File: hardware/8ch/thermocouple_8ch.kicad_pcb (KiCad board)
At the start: 4 copper layers, 250 x 140 mm, 208 parts, among them J1 24V_INPUT, J2 LCD_16x2_HEADER, J3 RELAY_COM_NO_NC, J4 RS485_A_B_GND_SHIELD, J5 AVR_ISP, J6 MCU_EXPANSION, K1 G5LE-1 DC24, Q1 2N7000, SW1 NEXT, SW2 UP, SW3 DOWN, SW4 SET, SW5 ACK, U1 ATmega32A-PU, U10 ISO7760FDWR, U11 ISO7761FDWR, U12 IA0505S, U13 LP2985-3.3, U14 LM5164DDAR, U15 ADM2587EBRWZ, U2 MAX31856MUD+, U3 MAX31856MUD+, U4 MAX31856MUD+, U5 MAX31856MUD+, U6 MAX31856MUD+, U7 MAX31856MUD+, U8 MAX31856MUD+, U9 MAX31856MUD+, Y1 8MHz 20pF

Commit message: Hierarchical schematic; U12 decoupling fixed; two blind gates fixed (I-062, I-045)
Schematic (I-062, decision 0019): an A3 root plus channel.kicad_sch (A4)
used by sheets TC1-TC8, derived by sch_layout/hier.py as the last step of
build.py. Only channel-internal nets were renamed (/TCn_X -> /TCn/X, 40
nets); JTC1-8 value -> K_TYPE (KiCad 10 keeps one value per symbol).
netlist_fingerprint.py --allow-renames proved all 645 pins on the same
nets; the baseline was regenerated from that netlist with the reason in it.
apply_rules.py patterns follow (without them: 499 isolation violations on a
test copy); board nets renamed in place by rename_board_nets.py.

Board (I-045): C45, U12's input cap, sat 55 mm away beside U10; C45/C46 now
sit under U12's pins, 18/10 mm -> 4.2 mm. Re-routed.

Gates that passed on the wrong input: close_gaps.py read a 2026-09-07 DRC
report (now runs its own with --refill-zones); check_mpn_consistency.py read
only the root after the split, 56 of 128 symbols (now follows every sheet
and runs inside validate.ps1, I-054 downgraded). populate_schematic.py
refuses the hierarchical root.

validate.ps1, KiCad 10.0.6: ERC 0/0, netlist IDENTICAL 201/162/645, MPN
128/128, DRC 0 errors / 0 warnings / 0 unconnected / 0 parity.
check_board.py all 6 ok. firmware/build.ps1: 3 suites pass.

Co-Authored-By: Claude Opus 5.5 <noreply@anthropic.com>
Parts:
- JTC1: value TC1_K_TYPE -> K_TYPE
- JTC2: value TC2_K_TYPE -> K_TYPE
- JTC3: value TC3_K_TYPE -> K_TYPE
- JTC4: value TC4_K_TYPE -> K_TYPE
- JTC5: value TC5_K_TYPE -> K_TYPE
- JTC6: value TC6_K_TYPE -> K_TYPE
- JTC7: value TC7_K_TYPE -> K_TYPE
- JTC8: value TC8_K_TYPE -> K_TYPE
- moved C45 58.8 mm to (153.2, 104.2), turned to 180 degrees
- moved C46 9.04 mm to (143.0, 104.2)
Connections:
- net /MISO_CH1 renamed /TC1/MISO_CH
- net /MISO_CH2 renamed /TC2/MISO_CH
- net /MISO_CH3 renamed /TC3/MISO_CH
- net /MISO_CH4 renamed /TC4/MISO_CH
- net /MISO_CH5 renamed /TC5/MISO_CH
- net /MISO_CH6 renamed /TC6/MISO_CH
- net /MISO_CH7 renamed /TC7/MISO_CH
- net /MISO_CH8 renamed /TC8/MISO_CH
- net /TC1_FILT_N renamed /TC1/FILT_N
- net /TC1_FILT_P renamed /TC1/FILT_P
- net /TC1_RAW_N renamed /TC1/RAW_N
- net /TC1_RAW_P renamed /TC1/RAW_P
- net /TC2_FILT_N renamed /TC2/FILT_N
- net /TC2_FILT_P renamed /TC2/FILT_P
- net /TC2_RAW_N renamed /TC2/RAW_N
- net /TC2_RAW_P renamed /TC2/RAW_P
- net /TC3_FILT_N renamed /TC3/FILT_N
- net /TC3_FILT_P renamed /TC3/FILT_P
- net /TC3_RAW_N renamed /TC3/RAW_N
- net /TC3_RAW_P renamed /TC3/RAW_P
- net /TC4_FILT_N renamed /TC4/FILT_N
- net /TC4_FILT_P renamed /TC4/FILT_P
- net /TC4_RAW_N renamed /TC4/RAW_N
- net /TC4_RAW_P renamed /TC4/RAW_P
- net /TC5_FILT_N renamed /TC5/FILT_N
- net /TC5_FILT_P renamed /TC5/FILT_P
- net /TC5_RAW_N renamed /TC5/RAW_N
- net /TC5_RAW_P renamed /TC5/RAW_P
- net /TC6_FILT_N renamed /TC6/FILT_N
- net /TC6_FILT_P renamed /TC6/FILT_P
- net /TC6_RAW_N renamed /TC6/RAW_N
- net /TC6_RAW_P renamed /TC6/RAW_P
- net /TC7_FILT_N renamed /TC7/FILT_N
- net /TC7_FILT_P renamed /TC7/FILT_P
- net /TC7_RAW_N renamed /TC7/RAW_N
- net /TC7_RAW_P renamed /TC7/RAW_P
- net /TC8_FILT_N renamed /TC8/FILT_N
- net /TC8_FILT_P renamed /TC8/FILT_P
- net /TC8_RAW_N renamed /TC8/RAW_N
- net /TC8_RAW_P renamed /TC8/RAW_P
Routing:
- net /CS7_SENS: track 77.8 -> 98.3 mm
- net /SPARE_PC4: track 63.0 -> 52.5 mm, vias 2 -> 0
- net /CS6_SENS: track 106.4 -> 116.1 mm
- net /CS8_SENS: track 70.6 -> 62.1 mm
- net /SPARE_PC5: track 53.3 -> 45.2 mm, vias 1 -> 0
- net /CS6_CTRL: track 87.5 -> 80.2 mm
- net /CS7_CTRL: track 67.2 -> 60.5 mm, vias 1 -> 0
- net /CS8_CTRL: track 64.9 -> 58.4 mm
- net /CS1_CTRL: track 32.9 -> 27.4 mm, vias 2 -> 1
- net /MISO_SENS: track 313.6 -> 308.5 mm, vias 9 -> 11
- net /GND_CTRL: track 81.8 -> 85.4 mm, vias 4 -> 5
- net /SCK_SENS: track 342.6 -> 346.0 mm, vias 11 -> 10
- net /MOSI_CTRL: track 58.8 -> 55.6 mm
- net /SCK_CTRL: track 66.5 -> 63.5 mm, vias 2 -> 1
- net /CS3_CTRL: track 36.5 -> 33.6 mm, vias 2 -> 0
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
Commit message: Close I-027 from the MAX31856 datasheet; silkscreen said REV A0 on REV A1
MAX31856 datasheet 19-7534 Rev 0 added (from LCSC C116632; analog.com resets
the workstation's connection). "T- is biased to approximately 0.735V by the
BIAS output" and the typical circuit is a floating thermocouple with BIAS on
T-, which every channel already has; BIAS floats between conversions and the
bank driver runs continuous mode. Ungrounded probes need no extra resistor.

The REV A1 board carried "THERMO-8CH REV A0" on its silkscreen: BOARD_REV was
never bumped. Now A1; place_labels() rewrites the revision line so
generate_board.py --silk-only carries a bump to a routed board.

validate.ps1: ERC 0/0, netlist IDENTICAL, MPN 128/128, DRC 0/0/0/0.

Co-Authored-By: Claude Opus 5.5 <noreply@anthropic.com>
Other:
- board text added: "THERMO-8CH REV A1 2026-09"
- board text removed: "THERMO-8CH REV A0 2026-09"
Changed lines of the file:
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@@
 		(tags "THT Terminal Block Phoenix MKDS-1,5-3 pitch 5mm size 15x9.8mm drill 1.3mm pad 2.6mm")
 		(property "Reference" "J3"
-			(at 5 -6.665 0)
+			(at 13.875 -0.305 0)
 			(layer "F.SilkS")
 			(effects
@@
 		)
 	)
-	(gr_text "THERMO-8CH  REV A0  2026-09"
+	(gr_text "THERMO-8CH  REV A1  2026-09"
 		(at 70 56.5 0)
 		(layer "F.SilkS")
@@
 	)
 	(gr_text "RUN-PERMIT\nDRY CONTACT"
-		(at 240.5 67.5 0)
+		(at 240.5 63.75 0)
 		(layer "F.SilkS")
 		(effects
@@
 	)
 	(gr_text "LOW-VOLTAGE\nLOAD ONLY"
-		(at 240.5 70.75 0)
+		(at 240.5 67 0)
 		(layer "F.SilkS")
 		(effects

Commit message: Schematic on six A4 sheets by function (0021); external panel fuse specified (0020)
The root's remaining blocks move to power, mcu, isolation and relay_rs485
sheets; the root becomes an A4 index beside the reused channel sheet.
56 sheet-internal nets gain the sheet path. apply_rules.py patterns and
board/units.bare() follow, and all 162 board nets keep their netclass.
Board nets renamed in place, copper unchanged. validate.ps1: ERC 0/0,
netlist IDENTICAL, MPN 128/128, DRC 0/0/0/0; check_board all ok; build.py
reproduces the six sheets.

I-028 (a): external 1 A time-delay DC fuse, >= 80 V DC, >= 10 kA, at the
battery end; inrush in CALCULATIONS.md 1.9. New low I-064 (board overlaps
its PCB-editor page frame, cosmetic).

Co-Authored-By: Claude Opus 5.5 <noreply@anthropic.com>
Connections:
- net /+24V_FUSED renamed /POWER/+24V_FUSED
- net /+24V_RAW renamed /POWER/+24V_RAW
- net /+5V_ISO renamed /ISOLATION/+5V_ISO
- net /+5V_RS485 renamed /RELAY_RS485/+5V_RS485
- net /AREF renamed /MCU/AREF
- net /BST_5V renamed /POWER/BST_5V
- net /BTN_ACK renamed /MCU/BTN_ACK
- net /BTN_DOWN renamed /MCU/BTN_DOWN
- net /BTN_NEXT renamed /MCU/BTN_NEXT
- net /BTN_SET renamed /MCU/BTN_SET
- net /BTN_UP renamed /MCU/BTN_UP
- net /CS1_SENS_RAW renamed /ISOLATION/CS1_SENS_RAW
- net /CS2_SENS_RAW renamed /ISOLATION/CS2_SENS_RAW
- net /CS3_SENS_RAW renamed /ISOLATION/CS3_SENS_RAW
- net /CS4_SENS_RAW renamed /ISOLATION/CS4_SENS_RAW
- net /CS5_SENS_RAW renamed /ISOLATION/CS5_SENS_RAW
- net /CS6_SENS_RAW renamed /ISOLATION/CS6_SENS_RAW
- net /CS7_SENS_RAW renamed /ISOLATION/CS7_SENS_RAW
- net /CS8_SENS_RAW renamed /ISOLATION/CS8_SENS_RAW
- net /FB_5V renamed /POWER/FB_5V
- net /GND_RS485 renamed /RELAY_RS485/GND_RS485
- net /LCD_D4 renamed /MCU/LCD_D4
- net /LCD_D5 renamed /MCU/LCD_D5
- net /LCD_D6 renamed /MCU/LCD_D6
- net /LCD_D7 renamed /MCU/LCD_D7
- net /LCD_E renamed /MCU/LCD_E
- net /LCD_LED_A renamed /MCU/LCD_LED_A
- net /LCD_RS renamed /MCU/LCD_RS
- net /LCD_VO renamed /MCU/LCD_VO
- net /MISO_SENS_RAW renamed /ISOLATION/MISO_SENS_RAW
- net /MOSI_SENS_RAW renamed /ISOLATION/MOSI_SENS_RAW
- net /RELAY_COM renamed /RELAY_RS485/RELAY_COM
- net /RELAY_GATE renamed /RELAY_RS485/RELAY_GATE
- net /RELAY_LED_A renamed /RELAY_RS485/RELAY_LED_A
- net /RELAY_LOW renamed /RELAY_RS485/RELAY_LOW
- net /RELAY_NC renamed /RELAY_RS485/RELAY_NC
- net /RELAY_NO renamed /RELAY_RS485/RELAY_NO
- net /RESET_N renamed /MCU/RESET_N
- net /RIPPLE_INJ renamed /POWER/RIPPLE_INJ
- net /RON_SET renamed /POWER/RON_SET
- net /RS485_A renamed /RELAY_RS485/RS485_A
- net /RS485_B renamed /RELAY_RS485/RS485_B
- net /RS485_BIAS_A renamed /RELAY_RS485/RS485_BIAS_A
- net /RS485_BIAS_B renamed /RELAY_RS485/RS485_BIAS_B
- net /RS485_RE_N renamed /RELAY_RS485/RS485_RE_N
- net /RS485_TERM_A renamed /RELAY_RS485/RS485_TERM_A
- net /SCK_SENS_RAW renamed /ISOLATION/SCK_SENS_RAW
- net /SPARE_PA2 renamed /MCU/SPARE_PA2
- net /SPARE_PA3 renamed /MCU/SPARE_PA3
- net /SPARE_PC3 renamed /MCU/SPARE_PC3
- net /SPARE_PC4 renamed /MCU/SPARE_PC4
- net /SPARE_PC5 renamed /MCU/SPARE_PC5
- net /SW_5V renamed /POWER/SW_5V
- net /VIN_UVLO renamed /POWER/VIN_UVLO
- net /XTAL1 renamed /MCU/XTAL1
- net /XTAL2 renamed /MCU/XTAL2

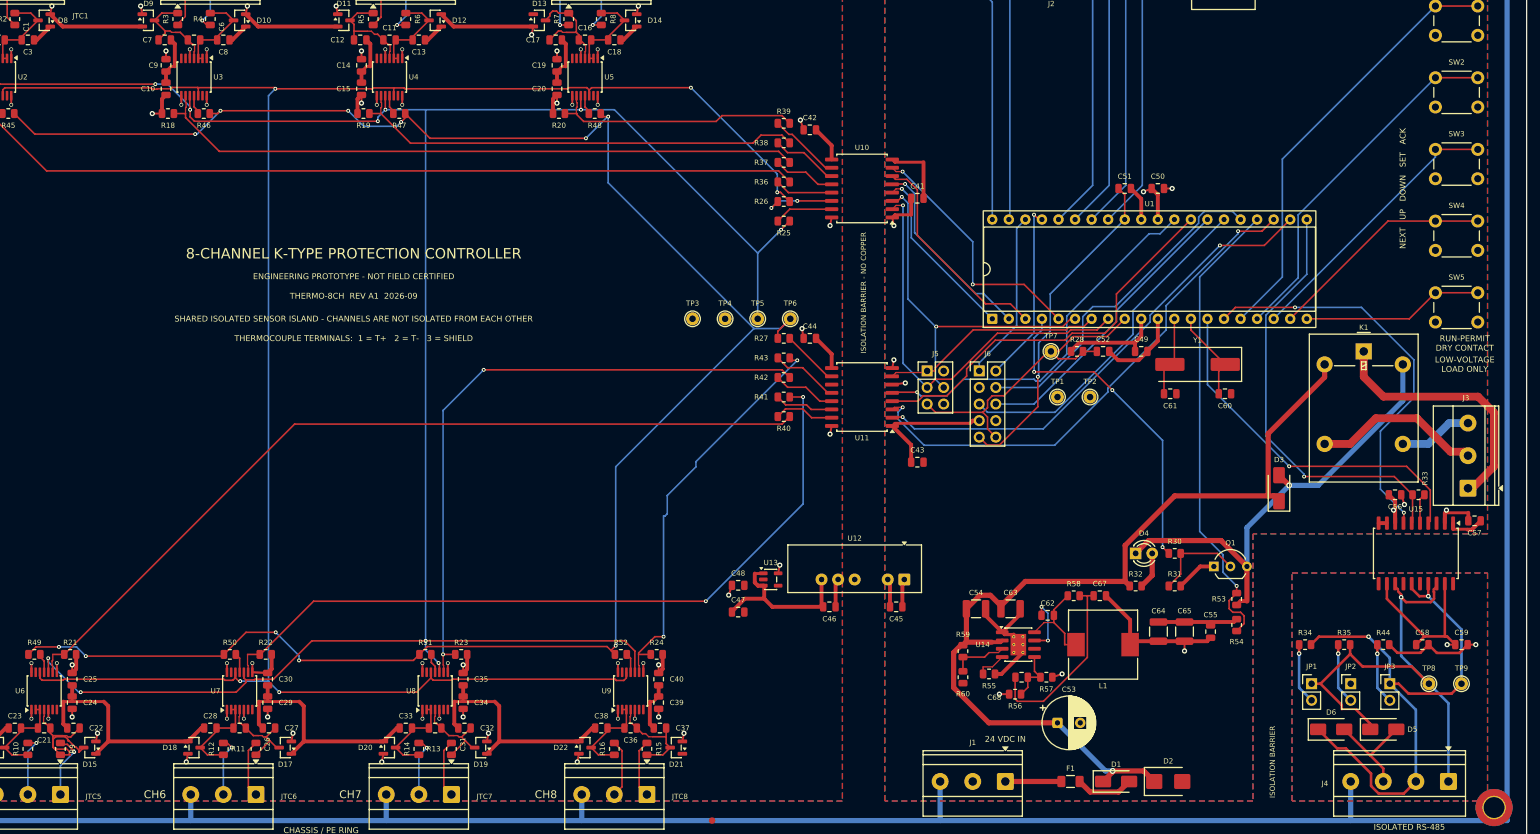
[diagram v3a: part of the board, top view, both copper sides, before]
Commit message: REV A2: pre-fabrication fixes I-065..I-069 (decision 0022)
- U10/U11 ISO7760DWR/ISO7761DWR (no F: open input -> HIGH) + R61 2k2 on
  U11 OUTF -> MISO_CTRL so in-circuit ISP works (I-065)
- Q1 BSS131 240 V SOT-23 replaces the 60 V 2N7000 (I-066)
- R53/R54 100k/22k: 0.28 mA into PC2's clamp at 58 V (I-067)
- F1 1812L075/60GR, 60 V 0.75 A 1812 (I-068)
- D2 drawn unidirectional, D3 = M7 SMA, U12 sourcing warning (I-069)
- netlist-baseline-reva2.json (202/163/647), BOARD_REV A2
- board regenerated and re-routed; one hand via for C41.1 (+5V_CTRL)
- run_all.ps1 no longer calls populate_schematic.py (hierarchical sheet)

validate.ps1 2026-09-28 01:07: ERC 0/0, netlist IDENTICAL, DRC 0/0/0/0;
check_board.py all 6 ok; firmware build + 3 suites pass.

Co-Authored-By: Claude Opus 5.5 <noreply@anthropic.com>
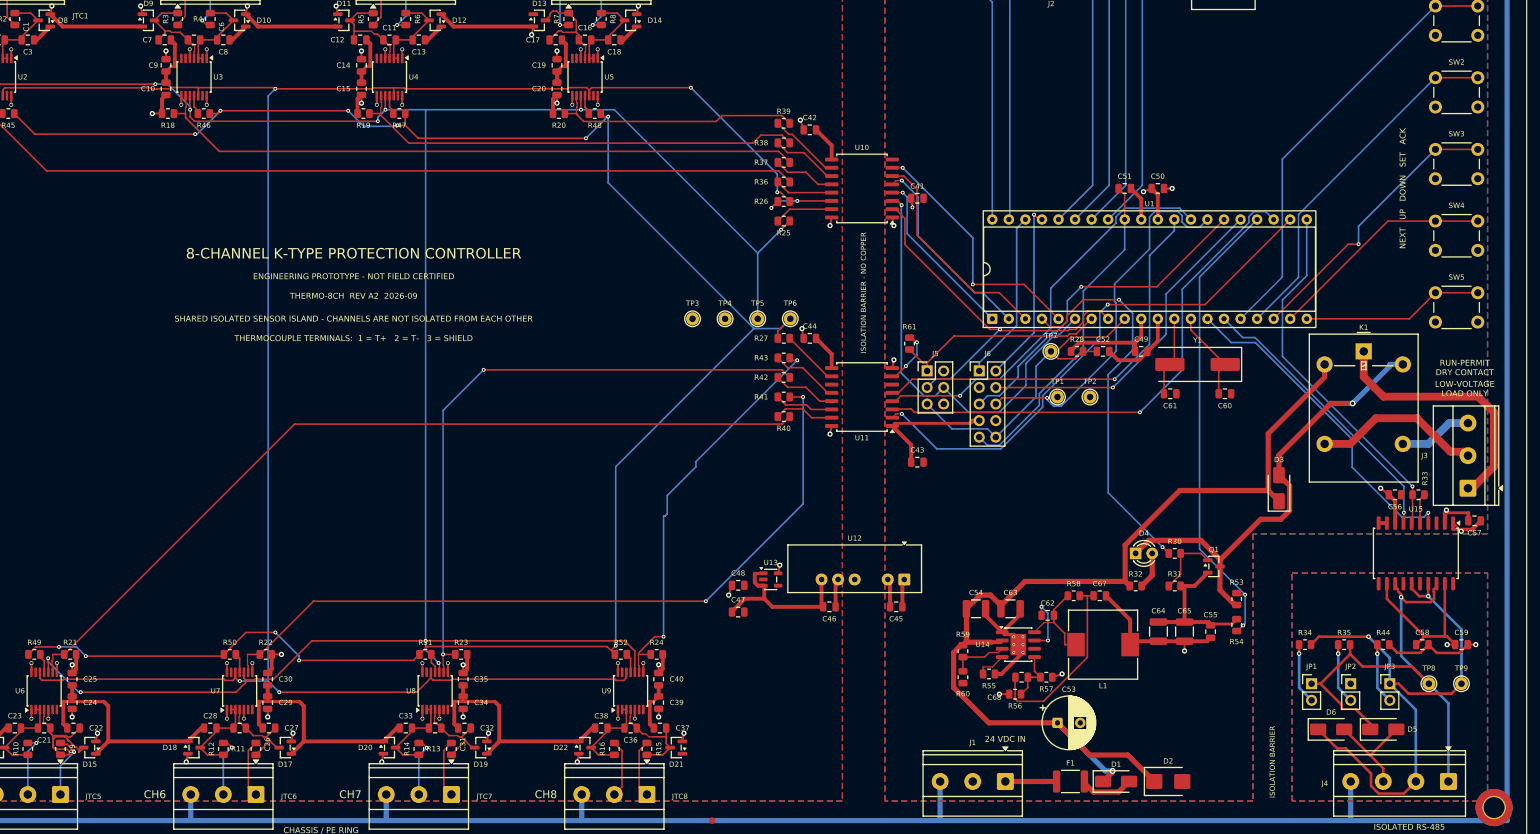
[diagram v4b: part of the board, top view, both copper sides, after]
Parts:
- added R61: 2k2, Resistor_SMD:R_0805_2012Metric, F.Cu at (155.3, 63.8)
- D3: value 1N4007 -> M7
- F1: value PTC 0.5A -> PTC 0.75A 60V; footprint Fuse:Fuse_1206_3216Metric -> Fuse:Fuse_1812_4532Metric
- Q1: value 2N7000 -> BSS131; footprint Package_TO_SOT_THT:TO-92_Inline_Wide -> Package_TO_SOT_SMD:SOT-23
- R53: value 22k -> 100k
- R54: value 4k7 -> 22k
- U10: value ISO7760FDWR -> ISO7760DWR
- U11: value ISO7761FDWR -> ISO7761DWR
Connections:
- Q1 pad 1: /GND_CTRL -> /RELAY_RS485/RELAY_GATE
- Q1 pad 2: /RELAY_RS485/RELAY_GATE -> /GND_CTRL
- U11 pad 7: /MISO_CTRL -> /ISOLATION/MISO_ISO
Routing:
- net /UART_TX: track 61.9 -> 43.9 mm, vias 2 -> 1
- net /MCU/SPARE_PC5: track 45.2 -> 57.3 mm, vias 0 -> 1
- net /+24V_PROT: track 143.7 -> 155.1 mm
- net /RS485_DE: track 66.7 -> 56.4 mm
- net /MOSI_CTRL: track 55.6 -> 65.6 mm, vias 2 -> 1
- net /RUN_PERMIT: track 50.4 -> 59.8 mm, vias 3 -> 2
- net /ISOLATION/MISO_ISO: track 0.00 -> 8.51 mm, vias 0 -> 2
- net /GND_CTRL: track 85.4 -> 77.2 mm, vias 5 -> 4
- net /CS5_CTRL: track 75.8 -> 81.5 mm
- net /UART_RX: track 56.2 -> 50.9 mm
- net /CS8_CTRL: track 58.4 -> 63.3 mm
- net /+5V_CTRL: track 95.3 -> 90.7 mm, vias 7 -> 8
- net /RELAY_RS485/RELAY_GATE: track 14.2 -> 10.3 mm
- net /SCK_CTRL: track 63.5 -> 60.4 mm
- net /CS7_CTRL: track 60.5 -> 63.0 mm, vias 0 -> 1
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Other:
- board text added: "THERMO-8CH REV A2 2026-09"
- board text removed: "THERMO-8CH REV A1 2026-09"
